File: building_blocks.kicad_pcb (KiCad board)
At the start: 2 copper layers, 48 x 65 mm, 54 parts, among them J1 conn_1x3, J10 conn_1x3, J2 conn_1x3, J3 conn_1x3, J5 conn_1x3, J6 conn_1x3, J7 conn_1x3, J8 conn_1x3, J9 conn_1x3, Q1 LBSS84LT1G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

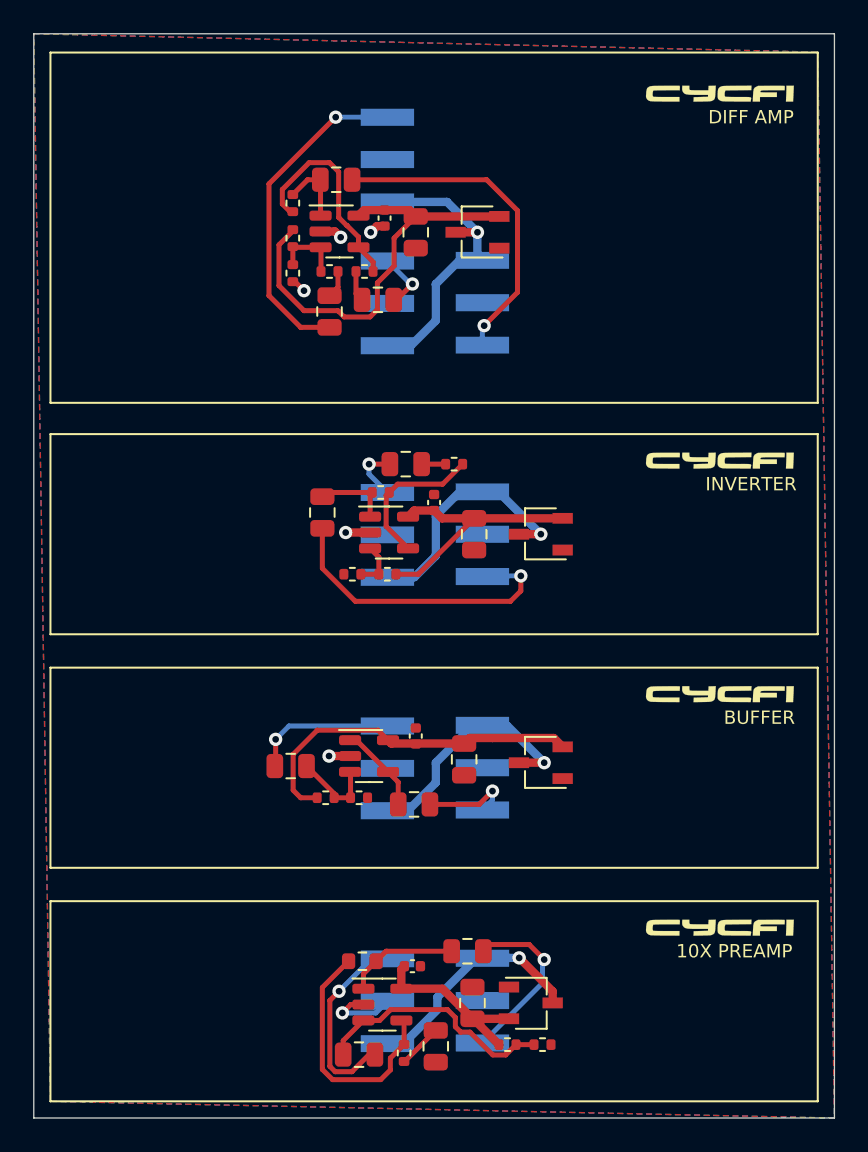
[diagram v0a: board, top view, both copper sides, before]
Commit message: Place all headers on top
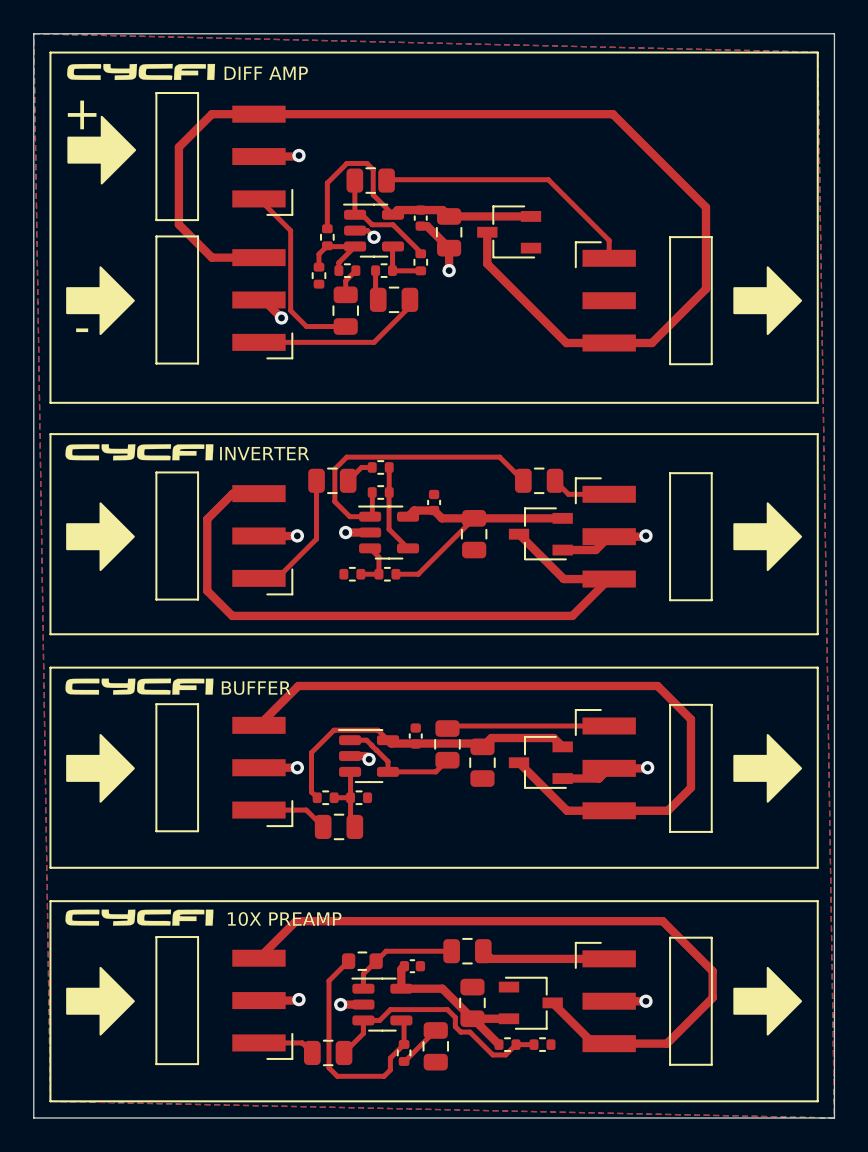
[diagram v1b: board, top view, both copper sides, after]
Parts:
- J1, J10, J2, J3, J5, J6, J7, J8, J9: moved to F.Cu
- moved G*** 34.8 mm to (101.3, 104.0)
- moved G*** 34.8 mm to (101.3, 76.1)
- moved G*** 34.8 mm to (101.3, 90.2)
- moved G*** 34.7 mm to (101.4, 53.3)
- moved C17 13.1 mm to (125.3, 77.8), turned to 0 degrees
- moved J7 9.26 mm to (108.5, 83.7)
- moved J5 9.21 mm to (129.5, 64.5)
- moved J3 9.21 mm to (108.5, 111.5)
- moved J8 9.20 mm to (108.5, 97.5)
- moved J1 9.13 mm to (108.5, 60.9)
- moved J10 9.12 mm to (129.5, 92.5)
- moved J6 9.12 mm to (129.5, 106.5)
- moved J2 9.11 mm to (108.5, 69.5)
- moved J9 9.06 mm to (129.5, 78.6)
- moved R7 8.45 mm to (118.2, 64.7)
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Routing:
- net v1+: track 18.4 -> 68.2 mm, vias 1 -> 0
- net v3+: track 14.7 -> 43.9 mm, vias 1 -> 0
- net v2+: track 14.0 -> 42.7 mm, vias 1 -> 0
- net v4+: track 15.1 -> 40.2 mm, vias 1 -> 0
- net GND: track 10.4 -> 33.1 mm, vias 6 -> 13
- net Net-(C17-Pad2): track 18.6 -> 3.58 mm, vias 1 -> 0
- net Net-(C17-Pad1): track 4.60 -> 18.1 mm
- net Net-(R2-Pad2): track 12.8 -> 3.16 mm
- net Net-(C3-Pad1): track 19.9 -> 11.2 mm, vias 1 -> 0
- net Net-(C2-Pad1): track 11.7 -> 3.45 mm, vias 1 -> 0
- net vcc1: track 25.8 -> 17.9 mm
- net Net-(C4-Pad1): track 3.58 -> 10.3 mm, vias 1 -> 0
- net Net-(C11-Pad1): track 3.41 -> 7.92 mm, vias 1 -> 0
- net Net-(C14-Pad1): track 8.65 -> 4.27 mm, vias 1 -> 0
- net Net-(C18-Pad2): track 5.47 -> 9.76 mm, vias 1 -> 0
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
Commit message: Move logo
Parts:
- moved G*** 30.6 mm to (131.9, 90.2)
- moved G*** 29.6 mm to (130.9, 76.1)
- moved G*** 29.6 mm to (131.0, 53.3)
- moved G*** 27.6 mm to (128.9, 104.0)
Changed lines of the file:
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@@
   )
   (footprint "cycfi_library:cycfi-logo-9mm" (layer "F.Cu")
-    (at 101.3 104)
+    (at 128.9 104)
     (attr through_hole board_only)
     (fp_text reference "G***" (at 0 0) (layer "F.SilkS") hide
@@
   )
   (footprint "cycfi_library:cycfi-logo-9mm" (layer "F.Cu")
-    (at 101.3 90.15)
+    (at 131.9 90.15)
     (attr through_hole board_only)
     (fp_text reference "G***" (at 0 0) (layer "F.SilkS") hide
@@
   )
   (footprint "cycfi_library:cycfi-logo-9mm" (layer "F.Cu")
-    (at 101.3 76.1)
+    (at 130.9 76.1)
     (attr through_hole board_only)
     (fp_text reference "G***" (at 0 0) (layer "F.SilkS") hide
@@
   )
   (footprint "cycfi_library:cycfi-logo-9mm" (layer "F.Cu")
-    (at 101.4 53.3)
+    (at 131 53.3)
     (attr through_hole board_only)
     (fp_text reference "G***" (at 0 0) (layer "F.SilkS") hide
@@
   (gr_rect (start 96 52.125) (end 142 73.125) (layer "F.SilkS") (width 0.12) (fill none))
   (gr_rect (start 95 51) (end 143 116) (layer "Edge.Cuts") (width 0.05) (fill none))
-  (gr_text "10X PREAMP" (at 110 104.1) (layer "F.SilkS")
+  (gr_text "10X PREAMP" (at 137.7 104.1) (layer "F.SilkS")
     (effects (font (size 0.8 0.8) (thickness 0.1)))
   )
@@
     (effects (font (size 2 2) (thickness 0.15)))
   )
-  (gr_text "DIFF AMP" (at 108.9 53.4) (layer "F.SilkS")
+  (gr_text "DIFF AMP" (at 138.6 53.4) (layer "F.SilkS")
     (effects (font (size 0.8 0.8) (thickness 0.1)))
   )
@@
     (effects (font (size 2 2) (thickness 0.15)))
   )
-  (gr_text "BUFFER" (at 108.3 90.25) (layer "F.SilkS")
+  (gr_text "BUFFER" (at 139 90.25) (layer "F.SilkS")
     (effects (font (size 0.8 0.8) (thickness 0.1)))
   )
-  (gr_text "INVERTER" (at 108.8 76.2) (layer "F.SilkS")
+  (gr_text "INVERTER" (at 138.5 76.2) (layer "F.SilkS")
     (effects (font (size 0.8 0.8) (thickness 0.1)))
   )

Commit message: refinements
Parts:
- moved R3 1.03 mm to (111.7, 62.7)
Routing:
- net GND: track 33.1 -> 37.9 mm, vias 13 -> 17
- net Net-(R1-Pad1): track 5.03 -> 6.59 mm

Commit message: More refinements
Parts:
- moved R6 10.1 mm to (115.5, 112.8), turned to -90 degrees
- moved R9 7.36 mm to (111.9, 107.0)
- moved C8 6.94 mm to (112.4, 109.9)
- moved C9 5.81 mm to (115.2, 106.3), turned to 90 degrees
- moved R4 4.39 mm to (119.6, 109.4), turned to -90 degrees
- moved C6 1.52 mm to (119.1, 107.5)
- moved R8 1.40 mm to (113.3, 106.5), turned to -90 degrees
- moved U2 0.92 mm to (116.5, 109.9)
- moved C1 0.70 mm to (121.3, 109.8), turned to -90 degrees
- moved C2 0.70 mm to (112.7, 112.8)
- moved Q1 0.70 mm to (124.8, 109.8), turned to 180 degrees
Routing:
- net Net-(C9-Pad2): track 7.74 -> 14.8 mm
- net Net-(C2-Pad2): track 14.6 -> 9.02 mm
- net Net-(R8-Pad1): track 14.3 -> 9.87 mm
- net Net-(C9-Pad1): track 6.74 -> 3.70 mm
- net v2+: track 42.7 -> 41.4 mm
- net Net-(C8-Pad1): track 2.67 -> 1.65 mm

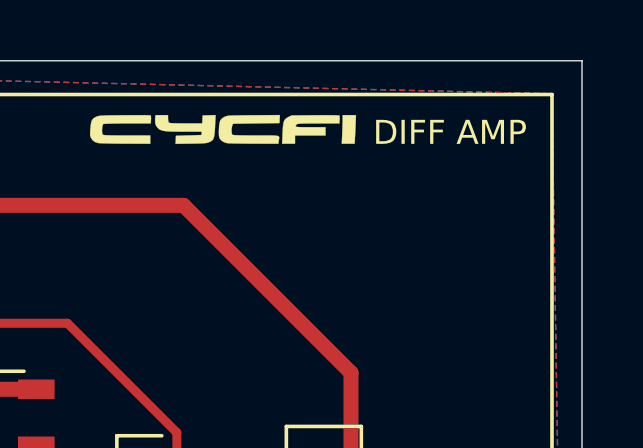
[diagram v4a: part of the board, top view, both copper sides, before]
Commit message: Added kikit fab script
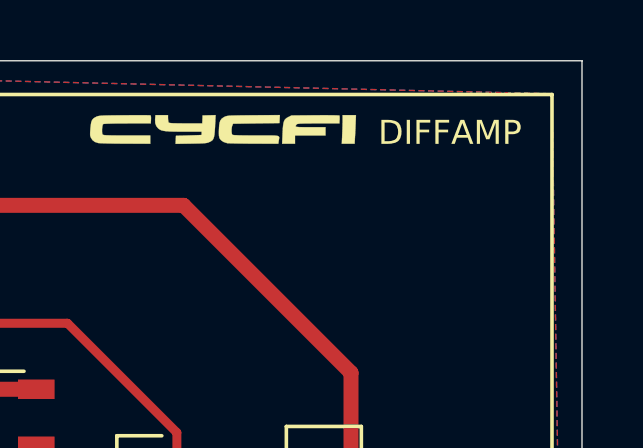
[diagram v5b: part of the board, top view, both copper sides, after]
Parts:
- R8: value 91k 0.1% -> 180k 0.1%
- R9: value 10k 1% -> 20k
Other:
- board text added: "DIFFAMP"
- board text removed: "DIFF AMP"
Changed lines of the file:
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@@
     (descr "Resistor SMD 0402 (1005 Metric), square (rectangular) end terminal, IPC_7351 nominal, (Body size source: IPC-SM-782 page 72, https://www.pcb-3d.com/wordpress/wp-content/uploads/ipc-sm-782a_amendment_1_and_2.pdf), generated with kicad-footprint-generator")
     (tags "resistor")
-    (property "LCSC" "C25744")
+    (property "LCSC" "C25765")
     (property "Sheetfile" "File: building_blocks.kicad_sch")
     (property "Sheetname" "")
@@
       (effects (font (size 1 1) (thickness 0.15)))
     )
-    (fp_text value "10k 1%" (at 0 1.17 90) (layer "F.Fab")
+    (fp_text value "20k" (at 0 1.17 90) (layer "F.Fab")
       (effects (font (size 1 1) (thickness 0.15)))
     )
@@
       (effects (font (size 1 1) (thickness 0.15)))
     )
-    (fp_text value "91k 0.1%" (at 0 1.43 90) (layer "F.Fab")
+    (fp_text value "180k 0.1%" (at 0 1.43 90) (layer "F.Fab")
       (effects (font (size 1 1) (thickness 0.15)))
     )
@@
     (effects (font (size 2 2) (thickness 0.15)))
   )
-  (gr_text "DIFF AMP" (at 138.6 53.4) (layer "F.SilkS")
+  (gr_text "DIFFAMP" (at 138.6 53.4) (layer "F.SilkS")
     (effects (font (size 0.8 0.8) (thickness 0.1)))
   )
